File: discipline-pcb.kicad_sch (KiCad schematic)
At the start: 169 parts, among them J1 AVR-ISP-6, SW1 KEYSW, SW10 KEYSW, SW11 KEYSW, SW12 KEYSW, SW13 KEYSW, SW14 KEYSW, SW15 KEYSW, SW16 KEYSW, SW17 KEYSW, SW18 KEYSW, SW19 KEYSW, SW2 KEYSW, SW20 KEYSW, SW21 KEYSW, SW22 KEYSW, SW23 KEYSW, SW24 KEYSW, SW25 KEYSW, SW26 KEYSW, SW27 KEYSW, SW28 KEYSW, SW29 KEYSW, SW3 KEYSW, SW30 KEYSW, SW31 KEYSW, SW32 KEYSW, SW33 KEYSW, SW34 KEYSW, SW35 KEYSW, SW36 KEYSW, SW37 KEYSW, SW38 KEYSW, SW39 KEYSW, SW4 KEYSW, SW40 KEYSW, SW41 KEYSW, SW42 KEYSW, SW43 KEYSW, SW44 KEYSW, SW45 KEYSW, SW46 KEYSW, SW47 KEYSW, SW48 KEYSW, SW49 KEYSW, SW5 KEYSW, SW50 KEYSW, SW51 KEYSW, SW52 KEYSW, SW53 KEYSW, SW54 KEYSW, SW55 KEYSW, SW56 KEYSW, SW57 KEYSW, SW58 KEYSW, SW59 KEYSW, SW6 KEYSW, SW60 KEYSW, SW61 KEYSW, SW62 KEYSW, SW63 KEYSW, SW64 KEYSW, SW65 KEYSW, SW66 KEYSW, SW67 KEYSW, SW68 KEYSW, SW69 KEYSW, SW7 KEYSW, SW70 KEYSW, SW71 KEYSW, SW72 KEYSW, SW73 KEYSW, SW74 KEYSW, SW75 KEYSW, SW76 KEYSW, SW77 KEYSW, SW78 KEYSW, SW8 KEYSW, SW9 KEYSW, U1 ATmega32A-PU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

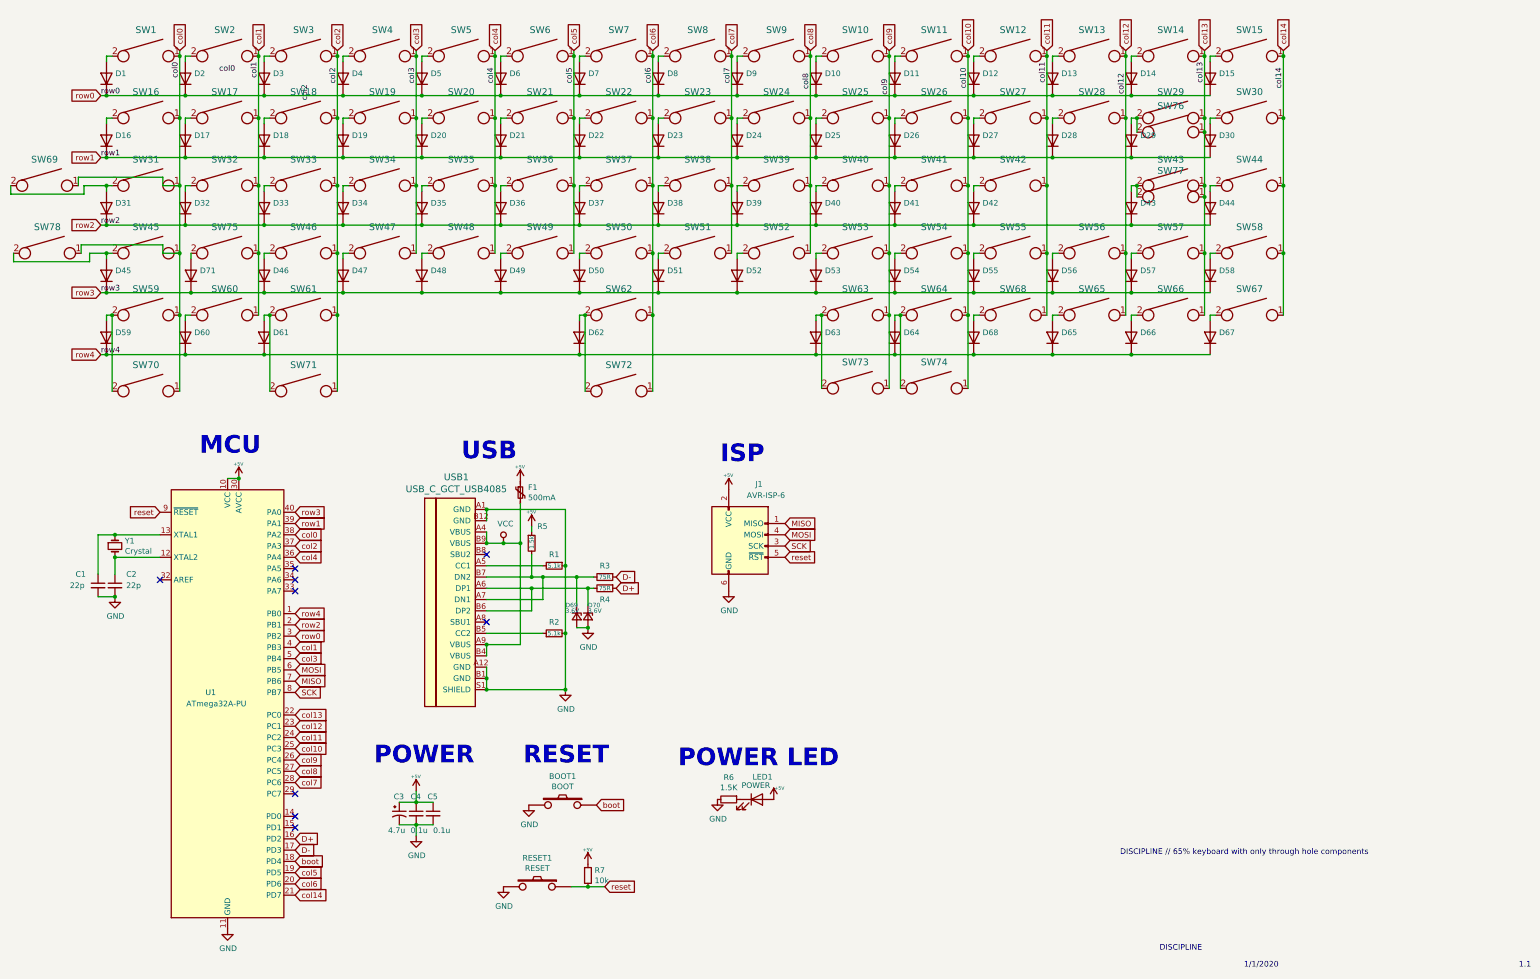
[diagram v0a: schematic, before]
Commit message: small schematic changes: lengthened two pins on MCU symbol to improve readability for silkscreen, snapped all symbols to grid
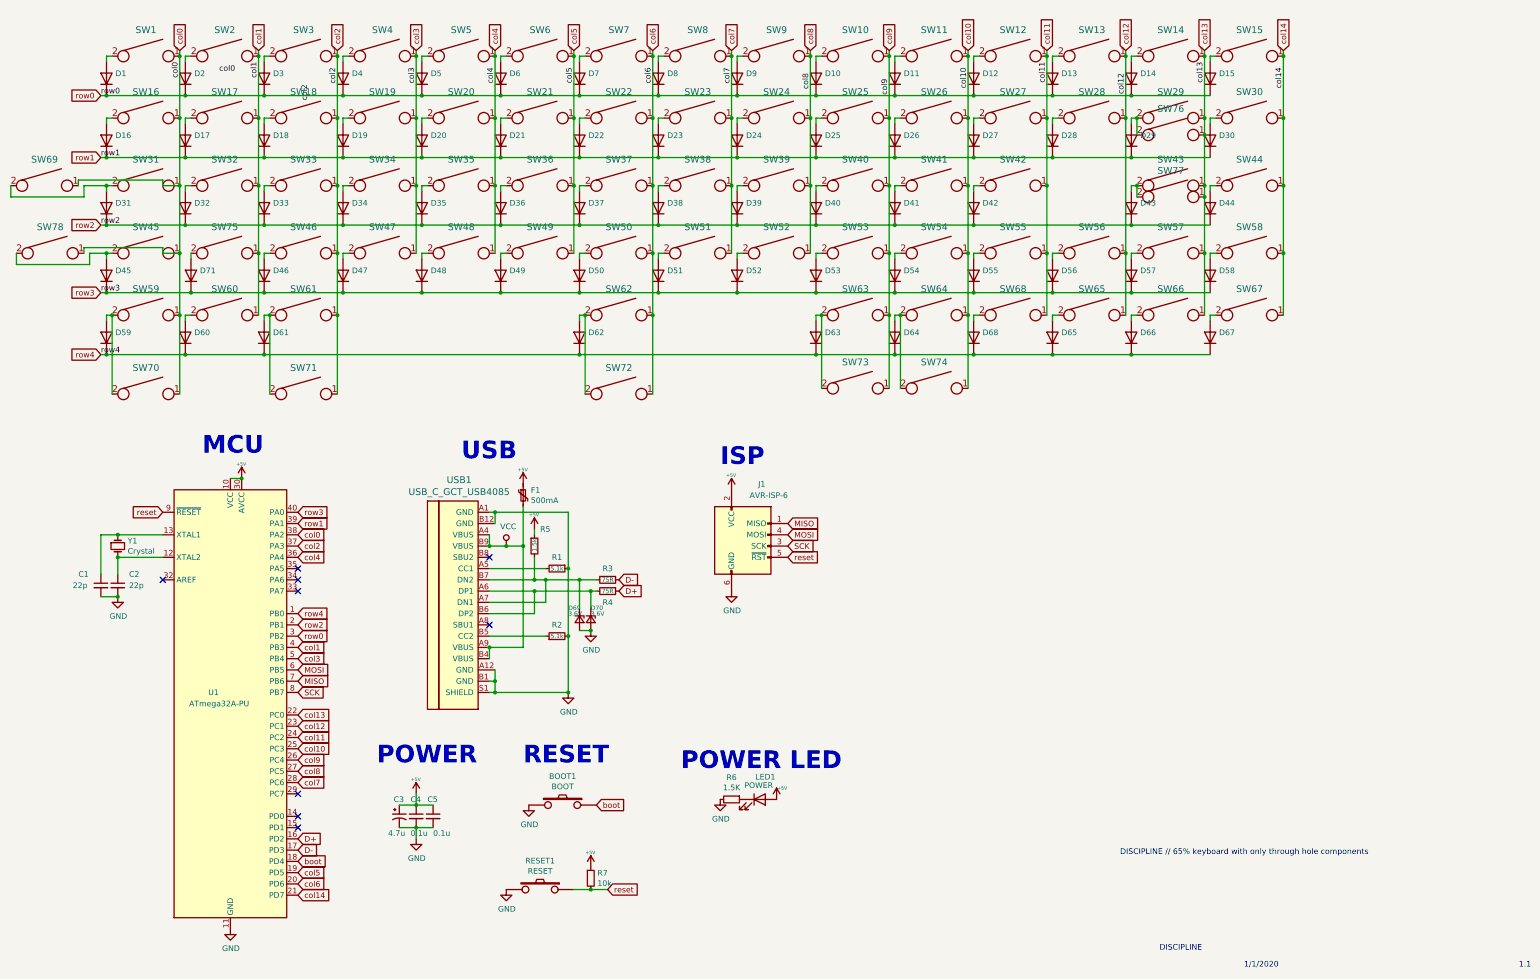
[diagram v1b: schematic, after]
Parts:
- D1, D10, D11, D12, D13, D14, D15, D16, D17, D18, D19, D2, D20, D21, D22, D23, D24, D25, D26, D27, D28, D29, D3, D30, D31, D32, D33, D34, D35, D36, D37, D38, D39, D4, D40, D41, D42, D43, D44, D45, D46, D47, D48, D49, D5, D50, D51, D52, D53, D54, D55, D56, D57, D58, D59, D6, D60, D61, D62, D63, D64, D65, D66, D67, D68, D7, D71, D8, D9: footprint cftkb:D_DO-35_SOD27_P5.08mm_Horizontal -> (none)
- SW1, SW10, SW11, SW12, SW13, SW15, SW17, SW18, SW19, SW2, SW20, SW21, SW22, SW23, SW24, SW25, SW26, SW27, SW28, SW3, SW30, SW32, SW33, SW34, SW35, SW36, SW37, SW38, SW39, SW4, SW40, SW41, SW42, SW44, SW46, SW47, SW48, SW49, SW5, SW50, SW51, SW52, SW53, SW54, SW55, SW57, SW58, SW6, SW62, SW65, SW66, SW67, SW68, SW7, SW72, SW75, SW77, SW8, SW9: footprint cftkb:SW_Cherry_MX1A_1.00u_PCB-NOSCREEN -> (none)
- SW14: footprint cftkb:SW_Cherry_MX1A_2.00u_PCBNOSCREEN -> (none)
- SW16, SW29, SW70, SW71, SW73, SW74: footprint cftkb:SW_Cherry_MX1A_1.50u_PCBNOSCREEN -> (none)
- SW31, SW56: footprint cftkb:SW_Cherry_MX1A_1.75u_PCBNOSCREEN -> (none)
- SW43, SW45: footprint cftkb:SW_Cherry_MX1A_2.25u_PCBNOSCREEN -> (none)
- SW59, SW60, SW61, SW63, SW64, SW69, SW78: footprint cftkb:SW_Cherry_MX1A_1.25u_PCBNOSCREEN -> (none)
- SW76: footprint cftkb:SW_Cherry_MX1A_ISOEnter_PCB_ReversedStabilizer -> (none)
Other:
- moved on the sheet: C1, C2, C3, C4, C5, D69, D70, F1, J1, LED1, R1, R2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
